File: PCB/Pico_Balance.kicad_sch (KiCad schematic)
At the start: 42 parts, among them J1 XT60PW-M, J2 GPIO_Ext, J3 Conn_Motor0, J4 Conn_Motor1, J5 USB_C_Receptacle_PowerOnly_6P, Q1 CSD17577Q3A, U1 BMI160, U2 DRV8876PWPR, U3 DRV8876PWPR, U4 LM74610QDGKRQ1, U5 LMR51430

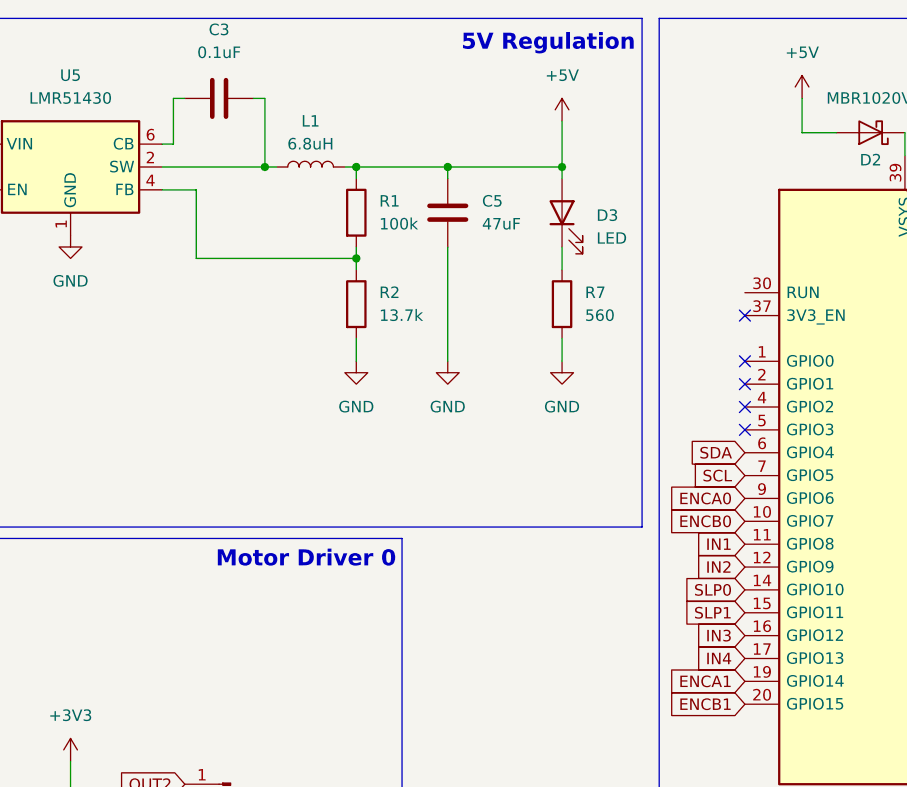
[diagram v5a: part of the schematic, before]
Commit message: Layout Refinements
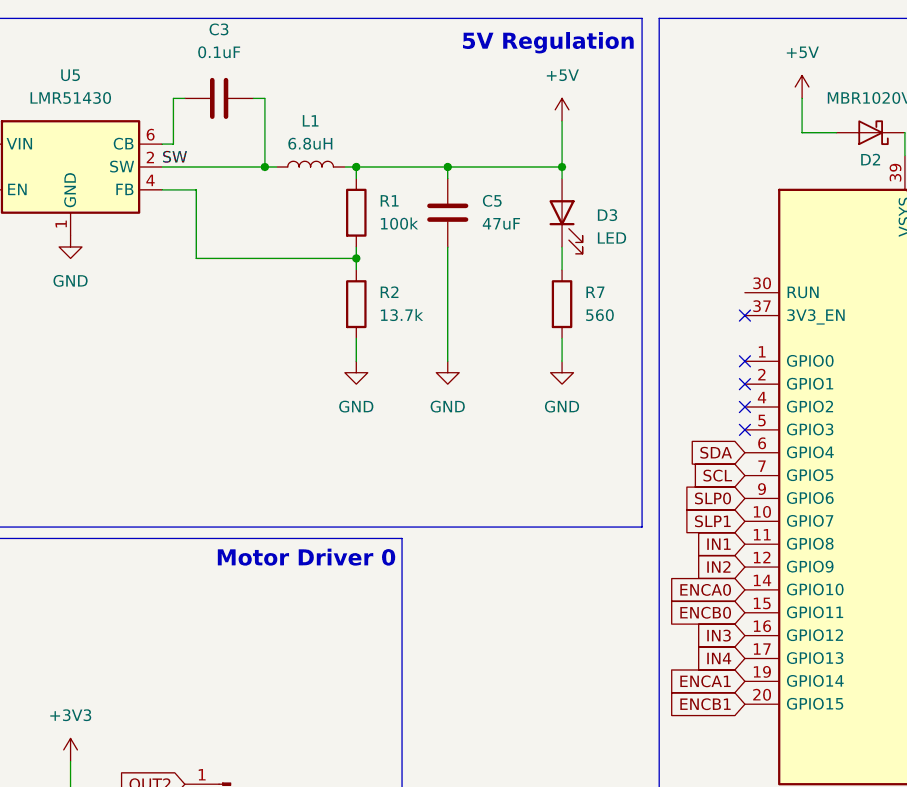
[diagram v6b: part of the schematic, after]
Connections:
- net ENCA0: now also A1.14 (GPIO10); no longer A1.9 (GPIO6)
- net ENCB0: now also A1.15 (GPIO11); no longer A1.10 (GPIO7)
- net SLP0: now also A1.9 (GPIO6); no longer A1.14 (GPIO10)
- net SLP1: now also A1.10 (GPIO7); no longer A1.15 (GPIO11)
- net SW: now reaches C3.2, L1.1, U5.2 (SW)

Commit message: First Round of Routing
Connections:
- net ENCA0: now also A1.16 (GPIO12); no longer A1.14 (GPIO10)
- net ENCB0: now also A1.17 (GPIO13); no longer A1.15 (GPIO11)
- net IN3: now also A1.14 (GPIO10); no longer A1.16 (GPIO12)
- net IN4: now also A1.15 (GPIO11); no longer A1.17 (GPIO13)
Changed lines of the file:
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@@
 	(global_label "ENCA0"
 		(shape input)
-		(at 207.01 76.2 180)
+		(at 207.01 81.28 180)
 		(fields_autoplaced yes)
 		(effects
@@
 		)
 		(property "Intersheetrefs" "${INTERSHEET_REFS}"
-			(at 197.9772 76.2 0)
+			(at 197.9772 81.28 0)
 			(effects
 				(font
@@
 	(global_label "IN3"
 		(shape input)
-		(at 207.01 81.28 180)
+		(at 207.01 76.2 180)
 		(fields_autoplaced yes)
 		(effects
@@
 		)
 		(property "Intersheetrefs" "${INTERSHEET_REFS}"
-			(at 200.88 81.28 0)
+			(at 200.88 76.2 0)
 			(effects
 				(font
@@
 	(global_label "ENCB0"
 		(shape input)
-		(at 207.01 78.74 180)
+		(at 207.01 83.82 180)
 		(fields_autoplaced yes)
 		(effects
@@
 		)
 		(property "Intersheetrefs" "${INTERSHEET_REFS}"
-			(at 197.7958 78.74 0)
+			(at 197.7958 83.82 0)
 			(effects
 				(font
@@
 	(global_label "IN4"
 		(shape input)
-		(at 207.01 83.82 180)
+		(at 207.01 78.74 180)
 		(fields_autoplaced yes)
 		(effects
@@
 		)
 		(property "Intersheetrefs" "${INTERSHEET_REFS}"
-			(at 200.88 83.82 0)
+			(at 200.88 78.74 0)
 			(effects
 				(font

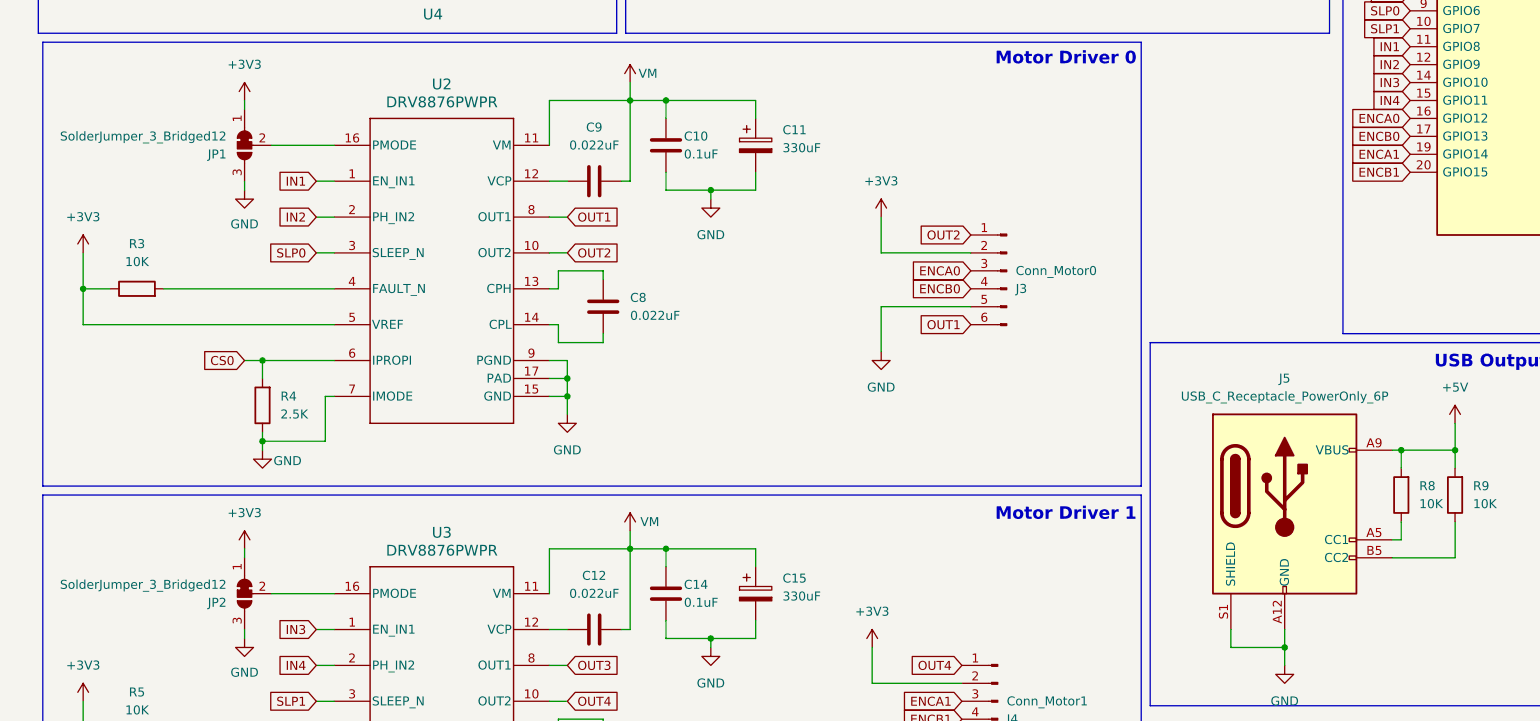
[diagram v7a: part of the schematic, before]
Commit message: Routing refinement and pour ground planes
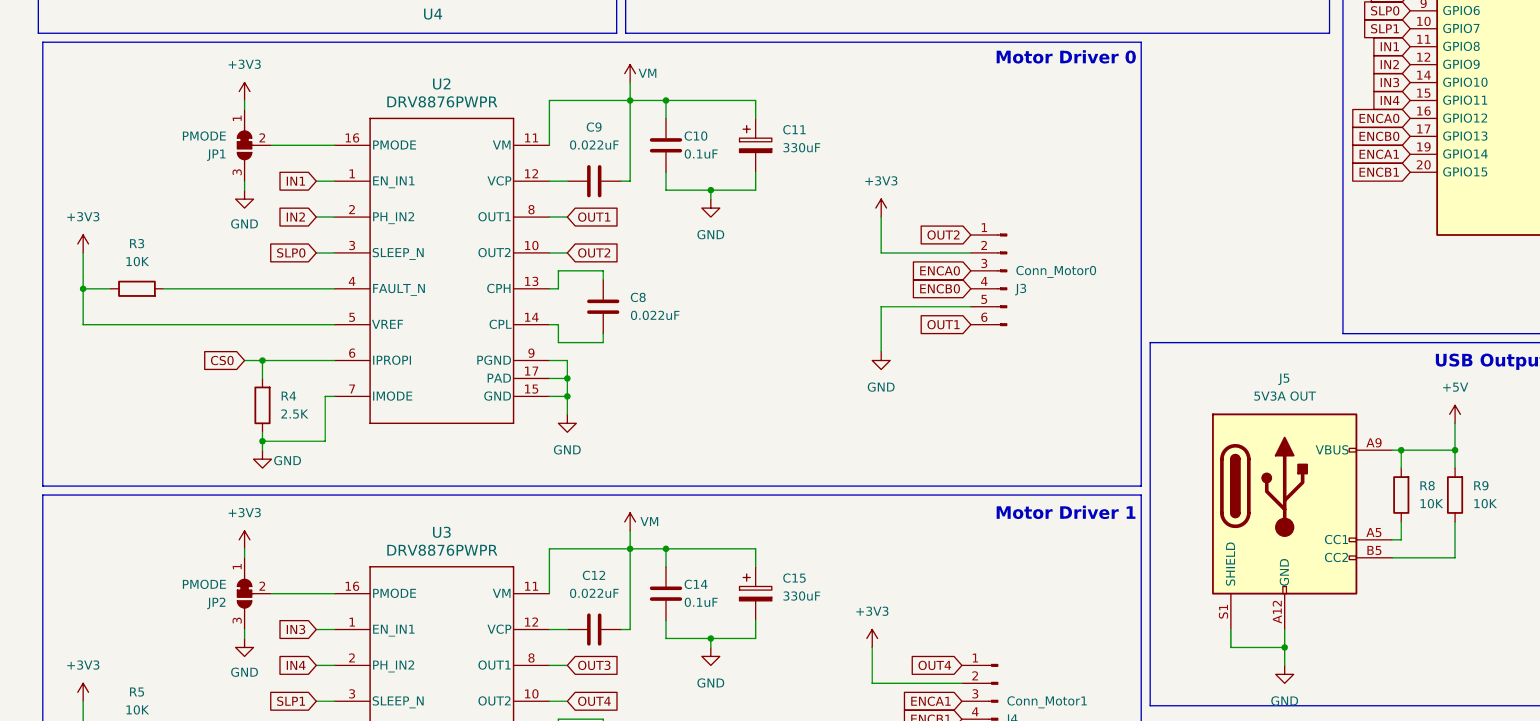
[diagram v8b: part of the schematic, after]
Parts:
- J5: value USB_C_Receptacle_PowerOnly_6P -> 5V3A OUT
- JP1, JP2: value SolderJumper_3_Bridged12 -> PMODE
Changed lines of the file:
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@@
 			)
 		)
-		(property "Value" "SolderJumper_3_Bridged12"
+		(property "Value" "PMODE"
 			(at 39.37 83.8201 90)
 			(effects
@@
 			)
 		)
-		(property "Value" "SolderJumper_3_Bridged12"
+		(property "Value" "PMODE"
 			(at 39.37 147.3201 90)
 			(effects
@@
 			)
 		)
-		(property "Value" "USB_C_Receptacle_PowerOnly_6P"
+		(property "Value" "5V3A OUT"
 			(at 189.23 120.65 0)
 			(effects
